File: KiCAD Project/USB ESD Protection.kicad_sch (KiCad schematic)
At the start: 5 parts, among them U10 USBLC6-2P6, U11 USBLC6-2P6, U12 USBLC6-2P6, U8 USBLC6-2P6, U9 USBLC6-2P6

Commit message: v1.0.0 RC2
Build candidate 2
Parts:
- U10, U11, U12, U8, U9: Mouser Price/Stock (none) -> https://www.mouser.com/ProductDetail/STMicroelectronics/USB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
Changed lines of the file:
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@@
+			)
+		)
+		(property "Mouser Price/Stock" "https://www.mouser.com/ProductDetail/STMicroelectronics/USBLC6-2P6?qs=6ARB0lp6jlViGcbUSvj1Mw%3D%3D"
+			(at 127 96.52 0)
+			(effects
+				(font
+					(size 1.27 1.27)
+				)
 			)
 		)
@@
 			)
 		)
+		(property "Mouser Price/Stock" "https://www.mouser.com/ProductDetail/STMicroelectronics/USBLC6-2P6?qs=6ARB0lp6jlViGcbUSvj1Mw%3D%3D"
+			(at 127 147.32 0)
+			(effects
+				(font
+					(size 1.27 1.27)
+				)
+			)
+		)
 		(pin "1"
 		)
@@
 			)
 		)
+		(property "Mouser Price/Stock" "https://www.mouser.com/ProductDetail/STMicroelectronics/USBLC6-2P6?qs=6ARB0lp6jlViGcbUSvj1Mw%3D%3D"
+			(at 127 121.92 0)
+			(effects
+				(font
+					(size 1.27 1.27)
+				)
+			)
+		)
 		(pin "1"
 		)
@@
 			)
 		)
+		(property "Mouser Price/Stock" "https://www.mouser.com/ProductDetail/STMicroelectronics/USBLC6-2P6?qs=6ARB0lp6jlViGcbUSvj1Mw%3D%3D"
+			(at 127 71.12 0)
+			(effects
+				(font
+					(size 1.27 1.27)
+				)
+			)
+		)
 		(pin "1"
 		)
@@
 			)
 		)
+		(property "Mouser Price/Stock" "https://www.mouser.com/ProductDetail/STMicroelectronics/USBLC6-2P6?qs=6ARB0lp6jlViGcbUSvj1Mw%3D%3D"
+			(at 127 45.72 0)
+			(effects
+				(font
+					(size 1.27 1.27)
+				)
+			)
+		)

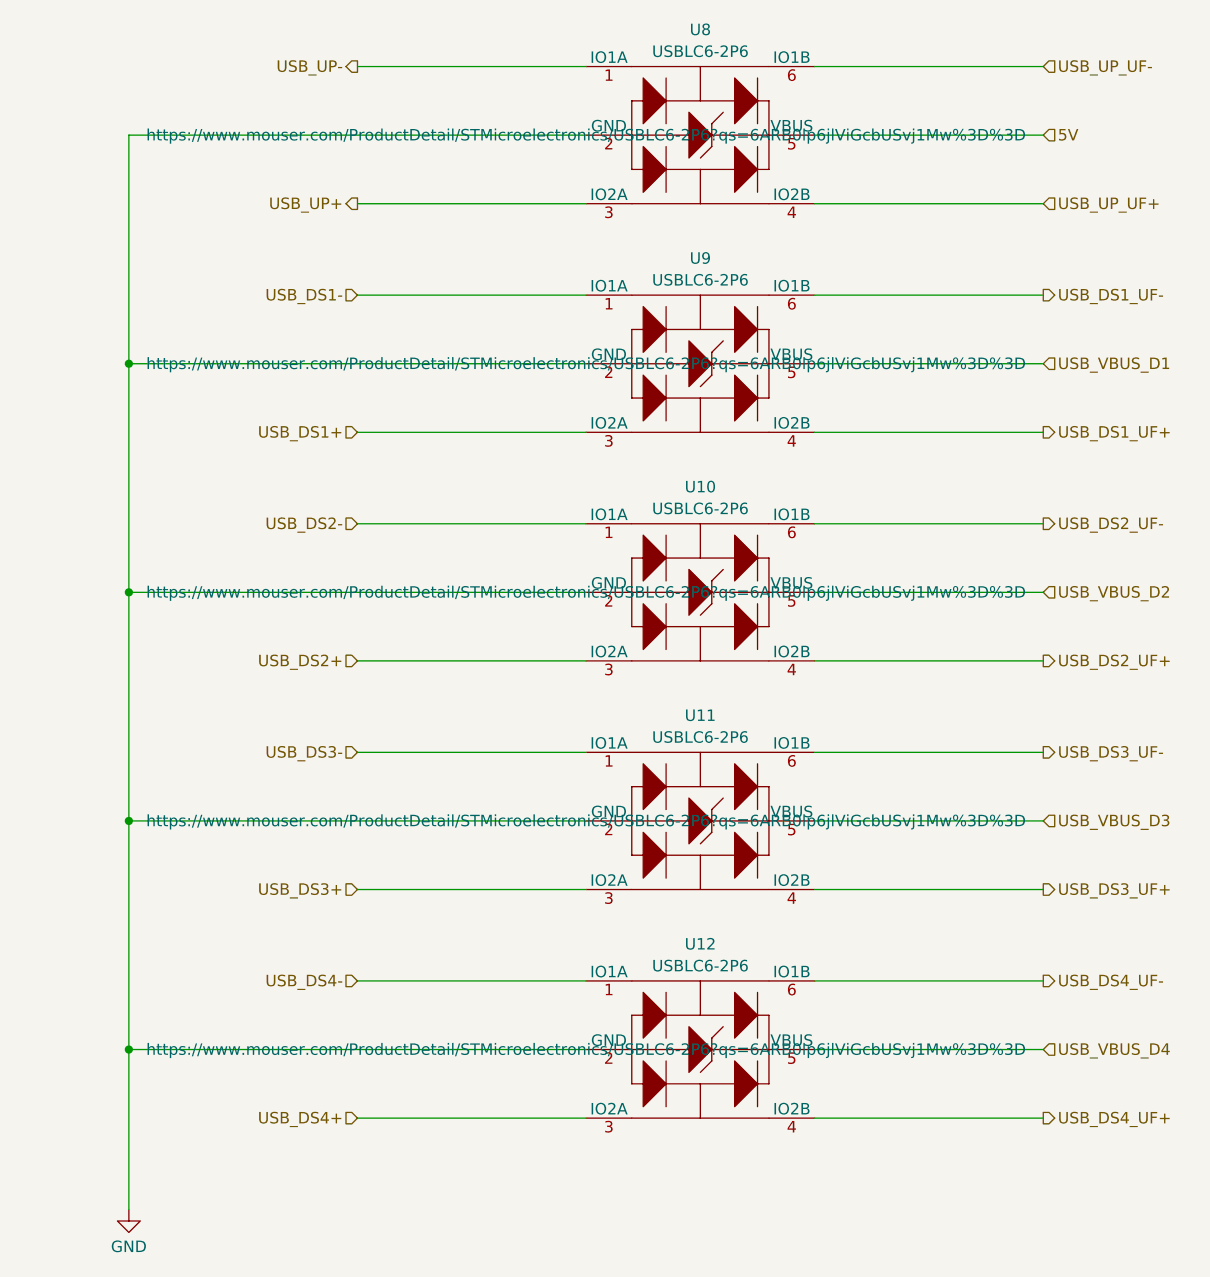
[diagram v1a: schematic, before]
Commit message: v1.0.0 RC3
Minor change to upstream USB port to connect Vbus to ESD protection vice on-board 5V.
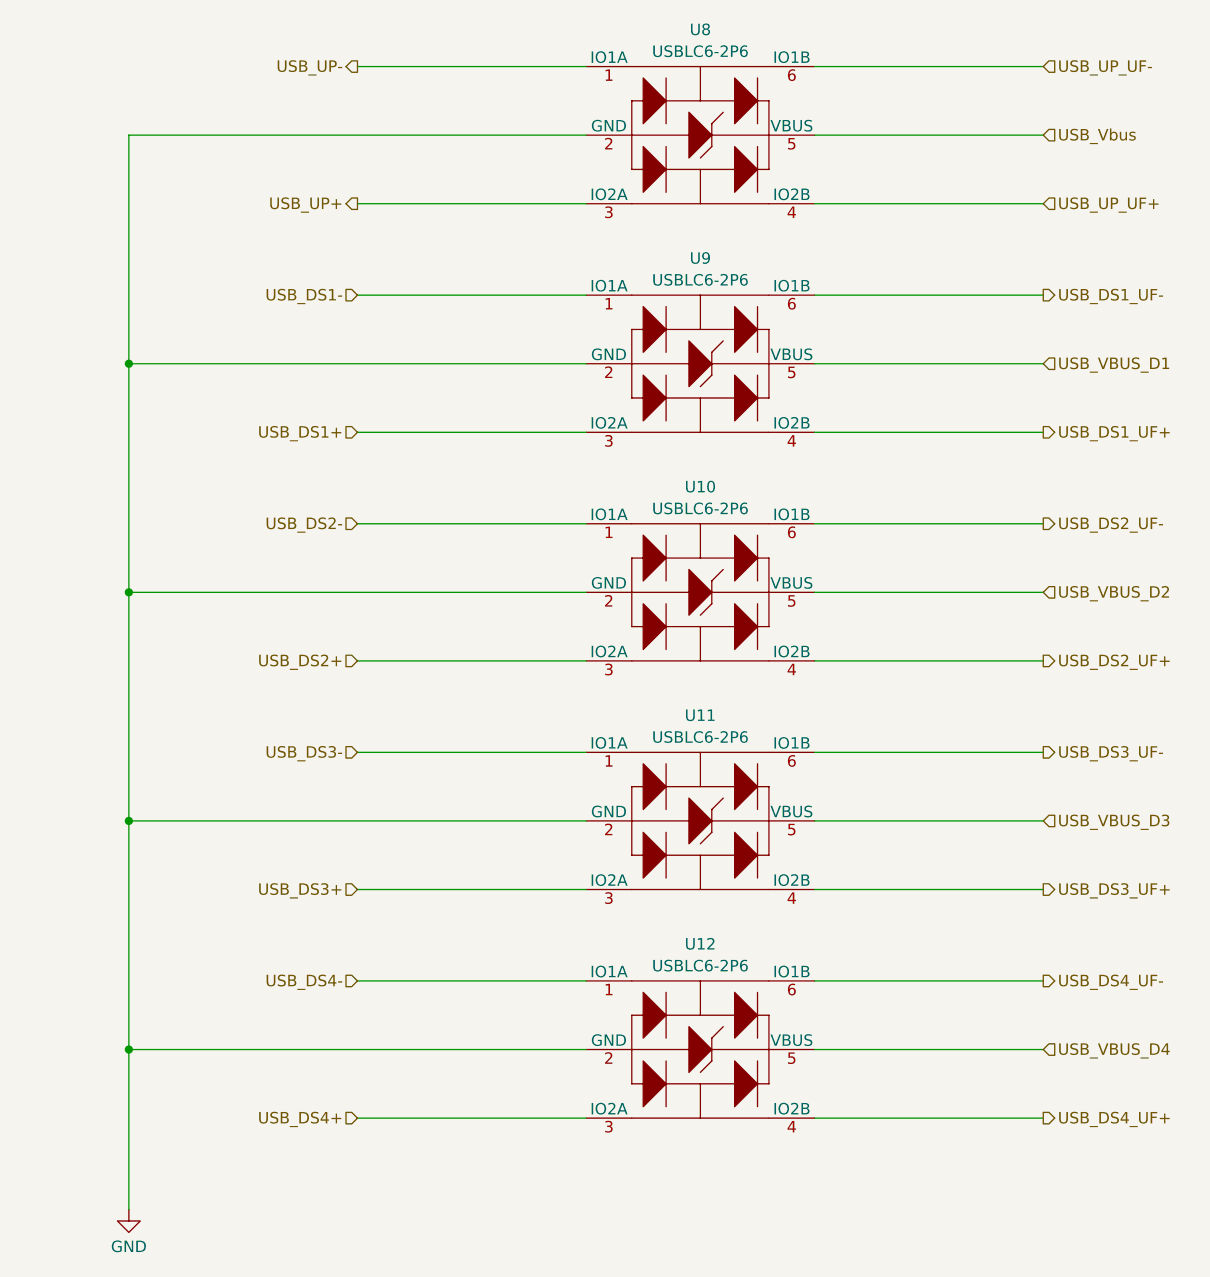
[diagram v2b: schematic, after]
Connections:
- net 5V renamed USB_Vbus
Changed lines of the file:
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@@
 		(title "1026 RPi Power Hat")
 		(date "2025-04-11")
-		(rev "1")
+		(rev "1.0.0 RC3")
 		(company "Dan Wilson")
 		(comment 1 "Copyright © 2025 Dan Wilson")
@@
 		)
 	)
-	(hierarchical_label "5V"
+	(hierarchical_label "USB_Vbus"
 		(shape input)
 		(at 177.8 45.72 0)
@@
 					(size 1.27 1.27)
 				)
+				(hide yes)
 			)
 		)
@@
 					(size 1.27 1.27)
 				)
+				(hide yes)
 			)
 		)
@@
 					(size 1.27 1.27)
 				)
+				(hide yes)
 			)
 		)
@@
 					(size 1.27 1.27)
 				)
+				(hide yes)
 			)
 		)
@@
 					(size 1.27 1.27)
 				)
-			)
-		)
+				(hide yes)
+			)
+		)

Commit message: v1.0.0A
Moved all symbols, footprints, and 3D models to local project-specific libraries in /KiCAD Project/Libraries.
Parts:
- U10, U11, U12, U8, U9: footprint DW_Semiconductors:[U] ST Micro USB ESD Protection USBLC6-2P6 -> 1026-3D:[U] ST Micro USB ESD Protection USBLC6-2P6; symbol DW_Semiconductors:[U] ST Micro USB ESD Protection USBLC6-2P6 -> 1026-3D:[U] ST Micro USB ESD Protection USBLC6-2P6
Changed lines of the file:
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@@
 	)
 	(symbol
-		(lib_id "power:GND")
+		(lib_id "1026-3D:GND")
 		(at 76.2 165.1 0)
 		(unit 1)
@@
 	)
 	(symbol
-		(lib_id "DW_Semiconductors:[U] ST Micro USB ESD Protection USBLC6-2P6")
+		(lib_id "1026-3D:[U] ST Micro USB ESD Protection USBLC6-2P6")
 		(at 127 96.52 0)
 		(unit 1)
@@
 			)
 		)
-		(property "Footprint" "DW_Semiconductors:[U] ST Micro USB ESD Protection USBLC6-2P6"
+		(property "Footprint" "1026-3D:[U] ST Micro USB ESD Protection USBLC6-2P6"
 			(at 152.4 183.82 0)
 			(effects
@@
 	)
 	(symbol
-		(lib_id "DW_Semiconductors:[U] ST Micro USB ESD Protection USBLC6-2P6")
+		(lib_id "1026-3D:[U] ST Micro USB ESD Protection USBLC6-2P6")
 		(at 127 147.32 0)
 		(unit 1)
@@
 			)
 		)
-		(property "Footprint" "DW_Semiconductors:[U] ST Micro USB ESD Protection USBLC6-2P6"
+		(property "Footprint" "1026-3D:[U] ST Micro USB ESD Protection USBLC6-2P6"
 			(at 152.4 234.62 0)
 			(effects
@@
 	)
 	(symbol
-		(lib_id "DW_Semiconductors:[U] ST Micro USB ESD Protection USBLC6-2P6")
+		(lib_id "1026-3D:[U] ST Micro USB ESD Protection USBLC6-2P6")
 		(at 127 121.92 0)
 		(unit 1)
@@
 			)
 		)
-		(property "Footprint" "DW_Semiconductors:[U] ST Micro USB ESD Protection USBLC6-2P6"
+		(property "Footprint" "1026-3D:[U] ST Micro USB ESD Protection USBLC6-2P6"
 			(at 152.4 209.22 0)
 			(effects
@@
 	)
 	(symbol
-		(lib_id "DW_Semiconductors:[U] ST Micro USB ESD Protection USBLC6-2P6")
+		(lib_id "1026-3D:[U] ST Micro USB ESD Protection USBLC6-2P6")
 		(at 127 71.12 0)
 		(unit 1)
@@
 			)
 		)
-		(property "Footprint" "DW_Semiconductors:[U] ST Micro USB ESD Protection USBLC6-2P6"
+		(property "Footprint" "1026-3D:[U] ST Micro USB ESD Protection USBLC6-2P6"
 			(at 152.4 158.42 0)
 			(effects
@@
 	)
 	(symbol
-		(lib_id "DW_Semiconductors:[U] ST Micro USB ESD Protection USBLC6-2P6")
+		(lib_id "1026-3D:[U] ST Micro USB ESD Protection USBLC6-2P6")
 		(at 127 45.72 0)
 		(unit 1)
@@
 			)
 		)
-		(property "Footprint" "DW_Semiconductors:[U] ST Micro USB ESD Protection USBLC6-2P6"
+		(property "Footprint" "1026-3D:[U] ST Micro USB ESD Protection USBLC6-2P6"
 			(at 152.4 133.02 0)
 			(effects
